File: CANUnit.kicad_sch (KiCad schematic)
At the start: 5 parts

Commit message: 回路図の作成
完成が見えてきた
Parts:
- added J? (x2): CANConn, Connector_JST:JST_XA_S04B-XASK-1_1x04_P2.50mm_Horizontal, symbol Connector:Conn_01x04_Socket
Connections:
- net CANH: now also J?.2 (Pin_2), J?.2 (Pin_2)
- net CANL: now also J?.3 (Pin_3), J?.3 (Pin_3)
- net GND: now also J?.4 (Pin_4), J?.4 (Pin_4)
- new net VCC: J?.1 (Pin_1), J?.1 (Pin_1)
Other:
- note added: "CAN_Flag"
- note added: "CAN_Unit"
- moved on the sheet: R?, SW?, U?

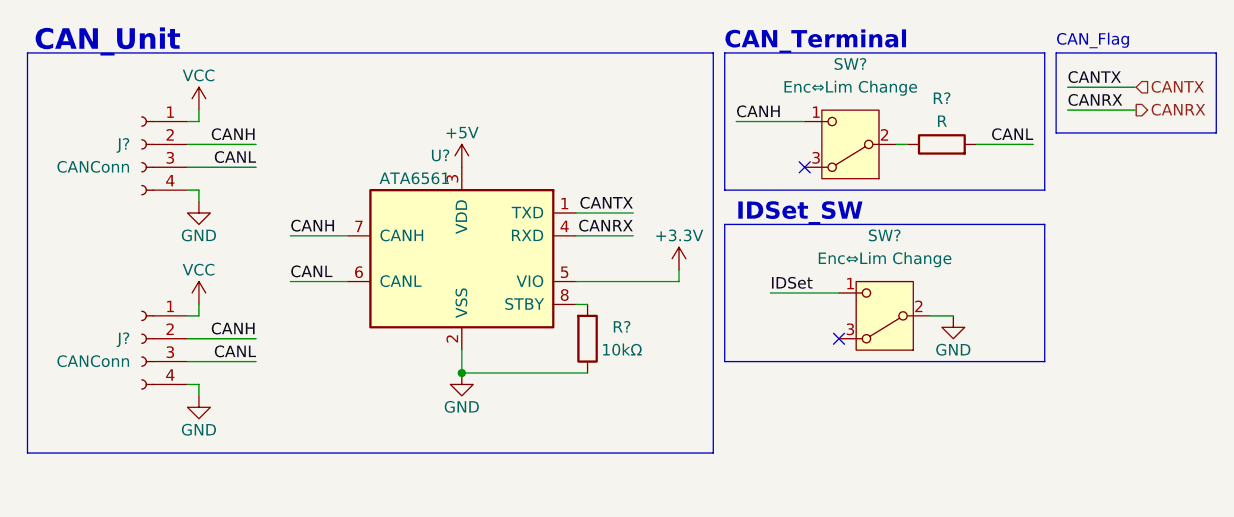
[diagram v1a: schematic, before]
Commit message: 回路図9割完成
回路図は9割完成
次からは配線作業をする
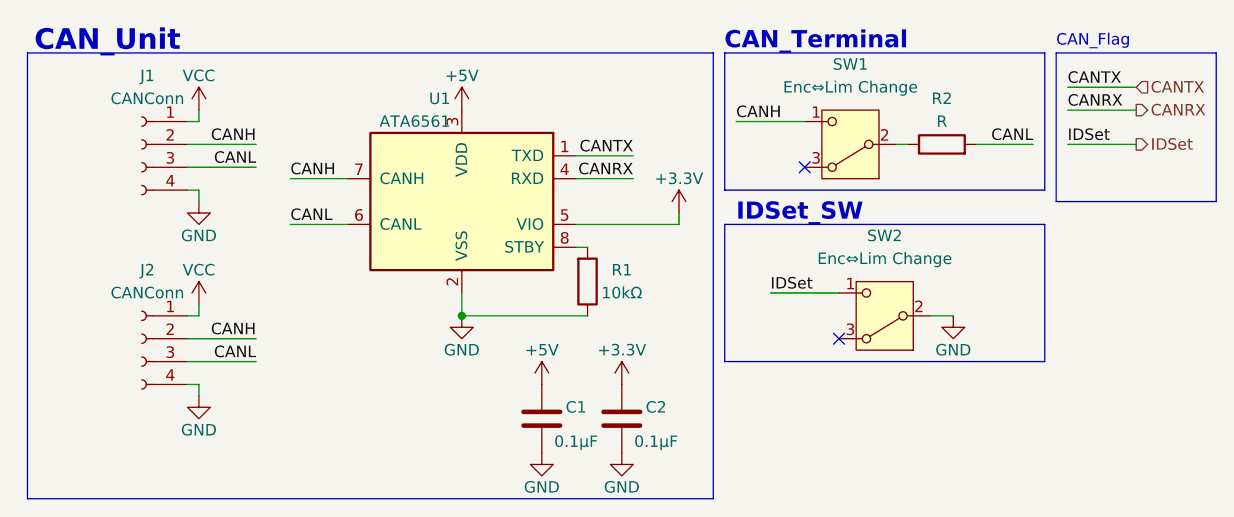
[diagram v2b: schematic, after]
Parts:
- added C1, C2: 0.1μF, Capacitor_SMD:C_0603_1608Metric, symbol Device:C
- gave numbers to parts that had none: 7
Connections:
- net +3.3V: now also C2.1
- net +5V: now also C1.1
- net GND: now also C1.2, C2.2
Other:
- moved on the sheet: R1, U1

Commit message: 回路図作った
リミットとエンコ共存いやかも
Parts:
- removed C1, C2: 0.1μF, Capacitor_SMD:C_0603_1608Metric, symbol Device:C
- removed J1, J2: CANConn, Connector_JST:JST_XA_S04B-XASK-1_1x04_P2.50mm_Horizontal, symbol Connector:Conn_01x04_Socket
- removed R1: 10kΩ, Resistor_SMD:R_0603_1608Metric, symbol Device:R
- removed R2: R, symbol Device:R
- removed SW1, SW2: Enc⇔Lim Change, Connector_PinHeader_2.54mm:PinHeader_1x03_P2.54mm_Vertical, symbol Switch:SW_Nidec_CAS-120A1
- removed U1: ATA6561, Package_SO:SOIC-8_3.9x4.9mm_P1.27mm, symbol Interface_CAN_LIN:MCP2551-I-SN
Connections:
- no-connect marks 2 -> 0
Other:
- note removed: "CAN_Flag"
- note removed: "CAN_Terminal"
- note removed: "CAN_Unit"
- note removed: "IDSet_SW"
